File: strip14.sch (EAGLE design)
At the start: 10 parts

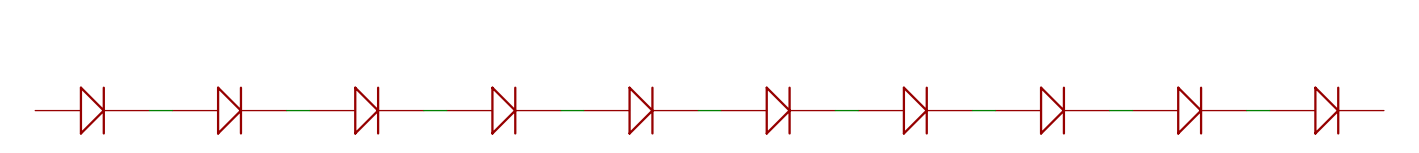
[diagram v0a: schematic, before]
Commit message: setts up warm cool LED support
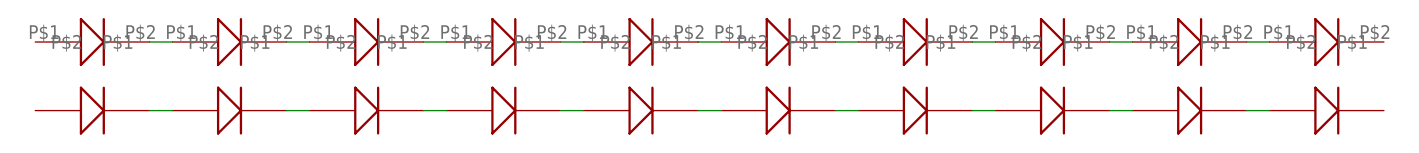
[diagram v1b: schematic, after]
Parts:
- added U$11, U$12, U$13, U$14, U$15, U$16, U$17, U$18, U$19, U$20: BXEN-40E-11M-3A-00-0-0, Smile_Shade:BXEN-40E-11M-3A-00-0-0
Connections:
- new net N$10: U$19.P$2, U$20.P$1
- new net N$11: U$18.P$2, U$19.P$1
- new net N$12: U$17.P$2, U$18.P$1
- new net N$13: U$16.P$2, U$17.P$1
- new net N$14: U$15.P$2, U$16.P$1
- new net N$15: U$11.P$2, U$12.P$1
- new net N$16: U$12.P$2, U$13.P$1
- new net N$17: U$13.P$2, U$14.P$1
- new net N$18: U$14.P$2, U$15.P$1
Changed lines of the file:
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@@
 <?xml version="1.0" encoding="utf-8"?>
 <!DOCTYPE eagle SYSTEM "eagle.dtd">
-<eagle version="8.0.0">
+<eagle version="8.0.2">
 <drawing>
 <settings>
@@
 <part name="U$9" library="Smile_Shade" deviceset="JDSTS2.EM-HRHT-XX52-1" device=""/>
 <part name="U$10" library="Smile_Shade" deviceset="JDSTS2.EM-HRHT-XX52-1" device=""/>
+<part name="U$11" library="Smile_Shade" deviceset="BXEN-40E-11M-3A-00-0-0" device=""/>
+<part name="U$12" library="Smile_Shade" deviceset="BXEN-40E-11M-3A-00-0-0" device=""/>
+<part name="U$13" library="Smile_Shade" deviceset="BXEN-40E-11M-3A-00-0-0" device=""/>
+<part name="U$14" library="Smile_Shade" deviceset="BXEN-40E-11M-3A-00-0-0" device=""/>
+<part name="U$15" library="Smile_Shade" deviceset="BXEN-40E-11M-3A-00-0-0" device=""/>
+<part name="U$16" library="Smile_Shade" deviceset="BXEN-40E-11M-3A-00-0-0" device=""/>
+<part name="U$17" library="Smile_Shade" deviceset="BXEN-40E-11M-3A-00-0-0" device=""/>
+<part name="U$18" library="Smile_Shade" deviceset="BXEN-40E-11M-3A-00-0-0" device=""/>
+<part name="U$19" library="Smile_Shade" deviceset="BXEN-40E-11M-3A-00-0-0" device=""/>
+<part name="U$20" library="Smile_Shade" deviceset="BXEN-40E-11M-3A-00-0-0" device=""/>
 </parts>
 <sheets>
@@
 <instance part="U$9" gate="G$1" x="129.54" y="5.08"/>
 <instance part="U$10" gate="G$1" x="144.78" y="5.08"/>
+<instance part="U$11" gate="G$1" x="7.62" y="12.7"/>
+<instance part="U$12" gate="G$1" x="22.86" y="12.7"/>
+<instance part="U$13" gate="G$1" x="38.1" y="12.7"/>
+<instance part="U$14" gate="G$1" x="53.34" y="12.7"/>
+<instance part="U$15" gate="G$1" x="68.58" y="12.7"/>
+<instance part="U$16" gate="G$1" x="83.82" y="12.7"/>
+<instance part="U$17" gate="G$1" x="99.06" y="12.7"/>
+<instance part="U$18" gate="G$1" x="114.3" y="12.7"/>
+<instance part="U$19" gate="G$1" x="129.54" y="12.7"/>
+<instance part="U$20" gate="G$1" x="144.78" y="12.7"/>
 </instances>
 <busses>
@@
 </segment>
 </net>
+<net name="N$10" class="0">
+<segment>
+<pinref part="U$20" gate="G$1" pin="P$1"/>
+<pinref part="U$19" gate="G$1" pin="P$2"/>
+<wire x1="137.16" y1="12.7" x2="134.62" y2="12.7" width="0.1524" layer="91"/>
+</segment>
+</net>
+<net name="N$11" class="0">
+<segment>
+<pinref part="U$19" gate="G$1" pin="P$1"/>
+<pinref part="U$18" gate="G$1" pin="P$2"/>
+<wire x1="121.92" y1="12.7" x2="119.38" y2="12.7" width="0.1524" layer="91"/>
+</segment>
+</net>
+<net name="N$12" class="0">
+<segment>
+<pinref part="U$18" gate="G$1" pin="P$1"/>
+<pinref part="U$17" gate="G$1" pin="P$2"/>
+<wire x1="106.68" y1="12.7" x2="104.14" y2="12.7" width="0.1524" layer="91"/>
+</segment>
+</net>
+<net name="N$13" class="0">
+<segment>
+<pinref part="U$17" gate="G$1" pin="P$1"/>
+<pinref part="U$16" gate="G$1" pin="P$2"/>
+<wire x1="91.44" y1="12.7" x2="88.9" y2="12.7" width="0.1524" layer="91"/>
+</segment>
+</net>
+<net name="N$14" class="0">
+<segment>
+<pinref part="U$16" gate="G$1" pin="P$1"/>
+<pinref part="U$15" gate="G$1" pin="P$2"/>
+<wire x1="76.2" y1="12.7" x2="73.66" y2="12.7" width="0.1524" layer="91"/>
+</segment>
+</net>
+<net name="N$15" class="0">
+<segment>
+<pinref part="U$11" gate="G$1" pin="P$2"/>
+<pinref part="U$12" gate="G$1" pin="P$1"/>
+<wire x1="12.7" y1="12.7" x2="15.24" y2="12.7" width="0.1524" layer="91"/>
+</segment>
+</net>
+<net name="N$16" class="0">
+<segment>
+<pinref part="U$12" gate="G$1" pin="P$2"/>
+<pinref part="U$13" gate="G$1" pin="P$1"/>
+<wire x1="27.94" y1="12.7" x2="30.48" y2="12.7" width="0.1524" layer="91"/>
+</segment>
+</net>
+<net name="N$17" class="0">
+<segment>
+<pinref part="U$13" gate="G$1" pin="P$2"/>
+<pinref part="U$14" gate="G$1" pin="P$1"/>
+<wire x1="43.18" y1="12.7" x2="45.72" y2="12.7" width="0.1524" layer="91"/>
+</segment>
+</net>
+<net name="N$18" class="0">
+<segment>
+<pinref part="U$14" gate="G$1" pin="P$2"/>
+<pinref part="U$15" gate="G$1" pin="P$1"/>
+<wire x1="58.42" y1="12.7" x2="60.96" y2="12.7" width="0.1524" layer="91"/>
+</segment>
+</net>
